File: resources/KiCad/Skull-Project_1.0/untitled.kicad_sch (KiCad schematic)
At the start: 1 part

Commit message: add Microwave Sensor for option two eyes
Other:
- title: Optional 2nd Eye -> Skull-Project 1.0
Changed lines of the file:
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@@
   (paper "A4")
   (title_block
-    (title "Optional 2nd Eye")
+    (title "Skull-Project 1.0")
     (date "2024-09-15")
     (rev "1.0")

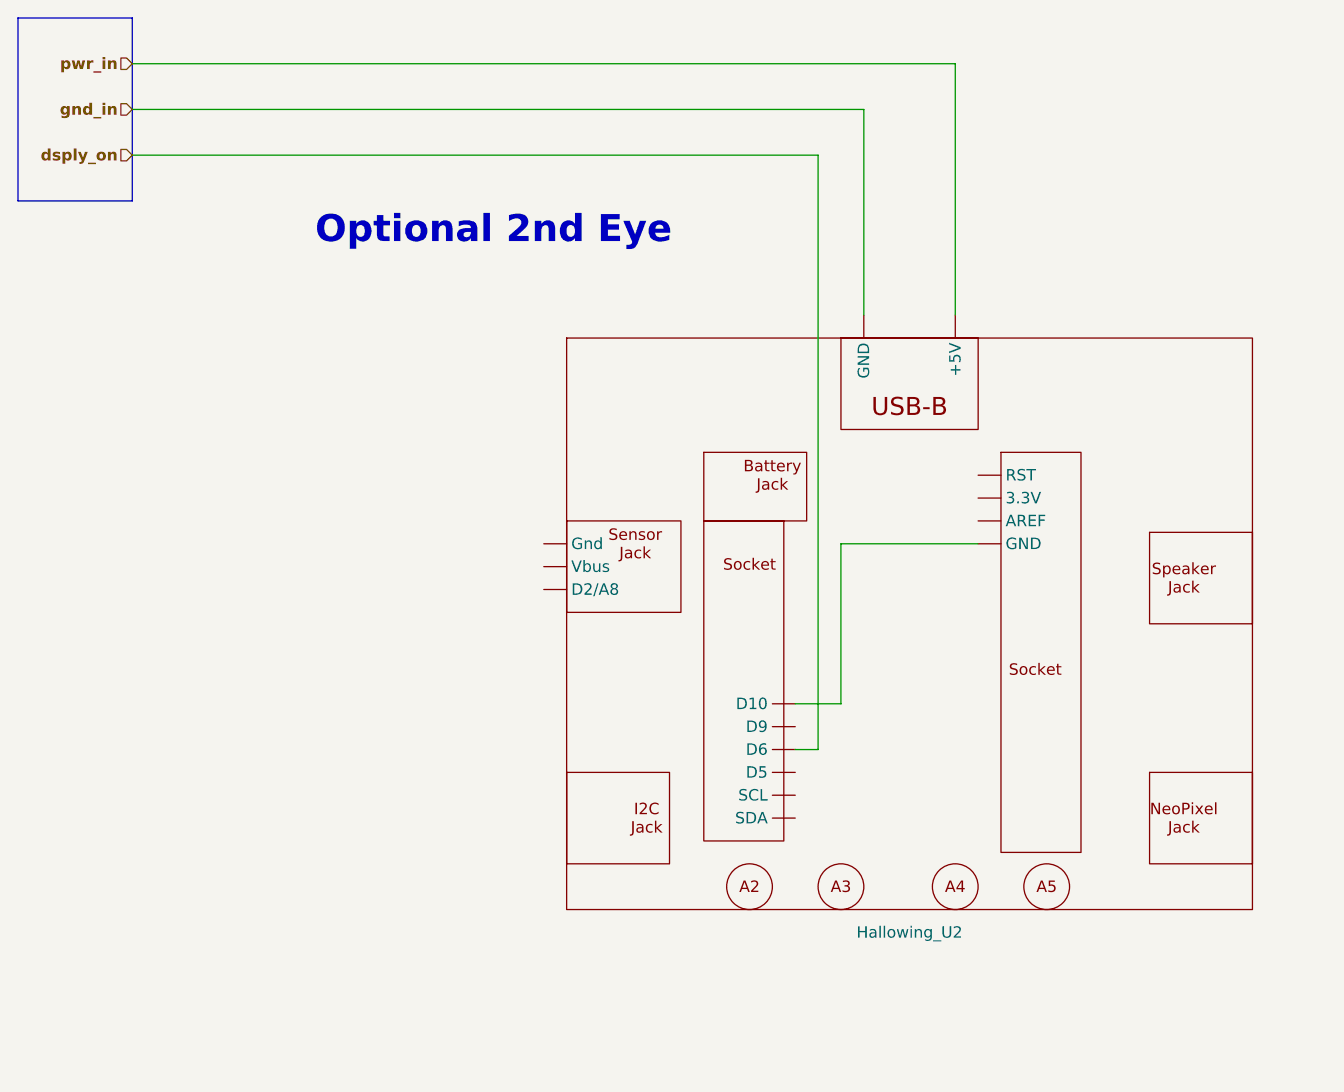
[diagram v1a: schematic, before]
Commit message: clean up schematic
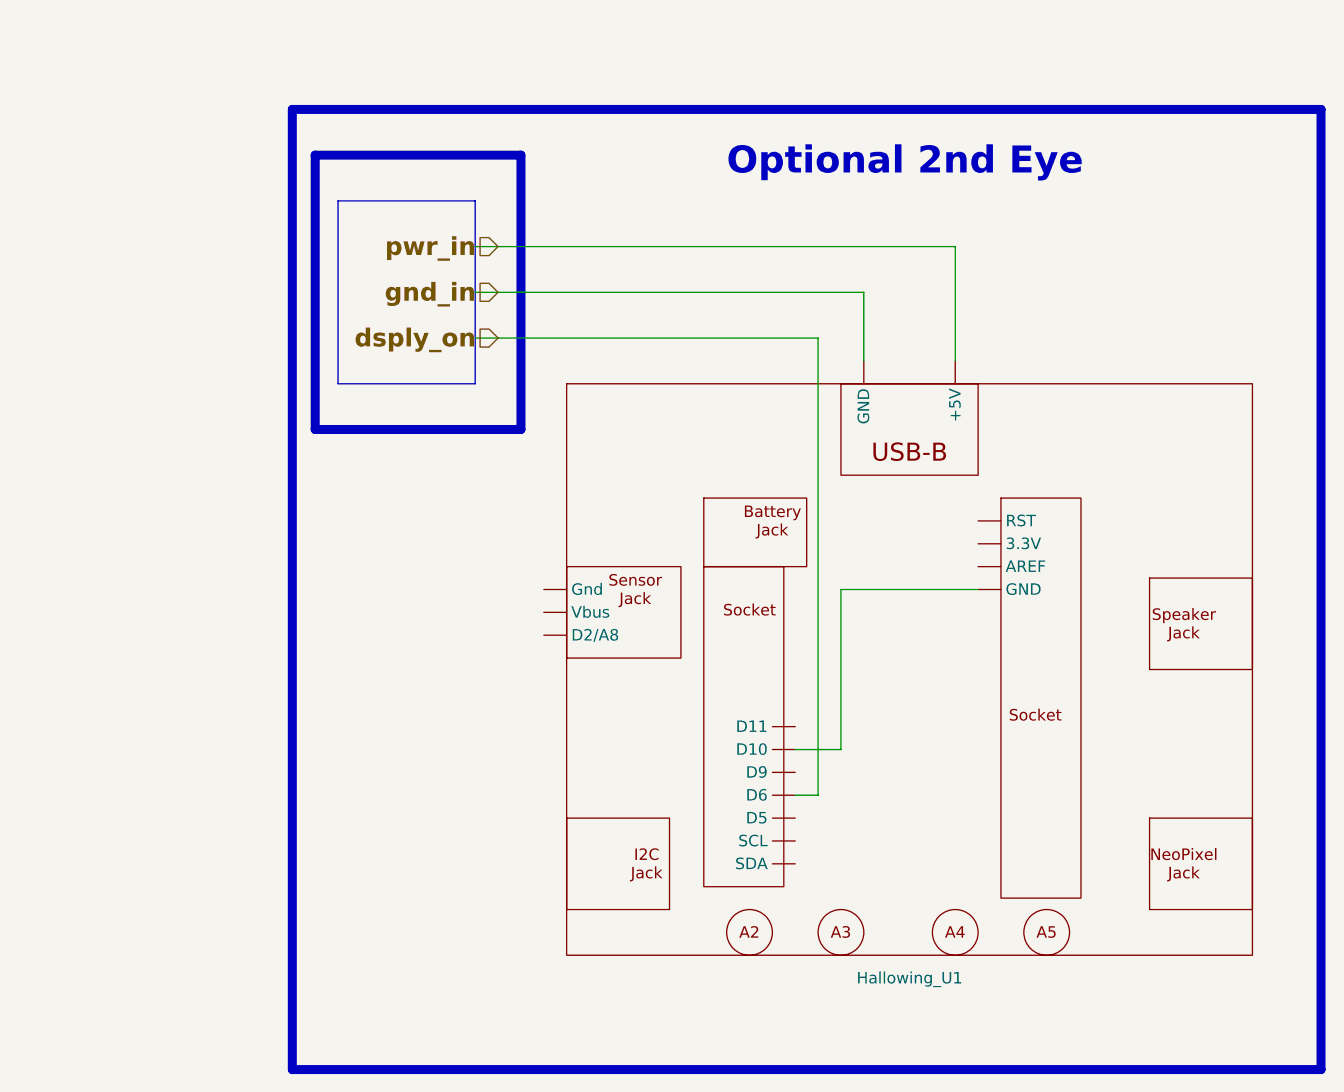
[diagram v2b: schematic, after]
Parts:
- removed Hallowing_U2: ~, symbol mdoLibrary:Hallowing_M4
- added Hallowing_U1: ~, symbol mdoLibrary:Hallowing_M4
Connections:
- net gnd_in: now also Hallowing_U1. (Vbus)
- net pwr_in: now also Hallowing_U1. (Vbus)
- new net dsply_on : Hallowing_U1. (Vbus)
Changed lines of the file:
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@@
     (comment 2 "NOTE: Hallowing as from display side (not connector side)")
   )
-  (wire (pts (xy 152.4 111.76) (xy 147.32 111.76))
+  (wire (pts (xy 152.4 116.84) (xy 147.32 116.84))
     (stroke (width 0) (type default))
   )
-  (wire (pts (xy 167.64 93.98) (xy 152.4 93.98))
+  (wire (pts (xy 165.1 60.96) (xy 165.1 73.66))
     (stroke (width 0) (type default))
   )
-  (wire (pts (xy 73.66 50.8) (xy 149.86 50.8))
+  (wire (pts (xy 167.64 99.06) (xy 152.4 99.06))
     (stroke (width 0) (type default))
   )
-  (wire (pts (xy 73.66 40.64) (xy 165.1 40.64))
+  (wire (pts (xy 149.86 71.12) (xy 149.86 121.92))
     (stroke (width 0) (type default))
   )
-  (wire (pts (xy 73.66 45.72) (xy 154.94 45.72))
+  (wire (pts (xy 111.76 71.12) (xy 149.86 71.12))
     (stroke (width 0) (type default))
   )
-  (wire (pts (xy 152.4 93.98) (xy 152.4 111.76))
+  (wire (pts (xy 152.4 99.06) (xy 152.4 116.84))
     (stroke (width 0) (type default))
   )
-  (wire (pts (xy 165.1 40.64) (xy 165.1 68.58))
+  (wire (pts (xy 111.76 60.96) (xy 165.1 60.96))
     (stroke (width 0) (type default))
   )
-  (wire (pts (xy 154.94 45.72) (xy 154.94 68.58))
+  (wire (pts (xy 154.94 66.04) (xy 154.94 73.66))
     (stroke (width 0) (type default))
   )
-  (wire (pts (xy 149.86 50.8) (xy 149.86 116.84))
+  (wire (pts (xy 111.76 66.04) (xy 154.94 66.04))
     (stroke (width 0) (type default))
   )
-  (wire (pts (xy 147.32 116.84) (xy 149.86 116.84))
+  (wire (pts (xy 147.32 121.92) (xy 149.86 121.92))
     (stroke (width 0) (type default))
   )
-  (rectangle (start 60.96 35.56) (end 73.66 55.88)
+  (rectangle (start 93.98 50.8) (end 116.84 81.28)
+    (stroke (width 1) (type default) (color 255 153 0 1))
+    (fill (type none))
+  )
+  (rectangle (start 96.52 55.88) (end 111.76 76.2)
     (stroke (width 0) (type default))
     (fill (type none))
   )
-  (text "Optional 2nd Eye" (at 93.98 60.96 0)
+  (rectangle (start 91.44 45.72) (end 205.74 152.4)
+    (stroke (width 1) (type default))
+    (fill (type none))
+  )
+  (rectangle (start 101.6 50.8) (end 101.6 50.8)
+    (stroke (width 0) (type default))
+    (fill (type none))
+  )
+  (text "Optional 2nd Eye" (at 139.7 53.34 0)
     (effects (font (size 3 3) (thickness 0.6) bold) (justify left bottom))
   )
-  (hierarchical_label "dsply_on" (shape input) (at 73.66 50.8 180) (fields_autoplaced)
-    (effects (font (size 1.27 1.27) bold) (justify right))
+  (hierarchical_label "dsply_on " (shape input) (at 114.3 71.12 180) (fields_autoplaced)
+    (effects (font (size 2 2) bold) (justify right))
   )
-  (hierarchical_label "gnd_in" (shape input) (at 73.66 45.72 180) (fields_autoplaced)
-    (effects (font (size 1.27 1.27) bold) (justify right))
+  (hierarchical_label "gnd_in" (shape input) (at 114.3 66.04 180) (fields_autoplaced)
+    (effects (font (size 2 2) bold) (justify right))
   )
-  (hierarchical_label "pwr_in" (shape input) (at 73.66 40.64 180) (fields_autoplaced)
-    (effects (font (size 1.27 1.27) bold) (justify right))
+  (hierarchical_label "pwr_in" (shape input) (at 114.3 60.96 180) (fields_autoplaced)
+    (effects (font (size 2 2) bold) (justify right))
   )
-  (symbol (lib_id "mdoLibrary:Hallowing_M4") (at 160.02 71.12 0) (unit 1)
+  (symbol (lib_name "Hallowing_M4_1") (lib_id "mdoLibrary:Hallowing_M4") (at 160.02 76.2 0) (unit 1)
     (in_bom yes) (on_board yes) (dnp no) (fields_autoplaced)
-    (property "Reference" "Hallowing_U2" (at 160.02 137.16 0)
+    (property "Reference" "Hallowing_U1" (at 160.02 142.24 0)
       (effects (font (size 1.27 1.27)))
     )
-    (property "Value" "~" (at 160.02 71.12 0)
+    (property "Value" "~" (at 160.02 76.2 0)
       (effects (font (size 1.27 1.27)))
     )
-    (property "Footprint" "" (at 160.02 71.12 0)
+    (property "Footprint" "" (at 160.02 76.2 0)
       (effects (font (size 1.27 1.27)) hide)
     )
-    (property "Datasheet" "" (at 160.02 71.12 0)
+    (property "Datasheet" "" (at 160.02 76.2 0)
       (effects (font (size 1.27 1.27)) hide)
     )
+    (pin "")
     (pin "")
     (pin "")
@@
       (project "Skull-Project_1.0"
         (path "/13d7b3b4-5d80-4b2f-98bb-c8334b3eaf59/dd2fe223-2832-49f4-937d-cadfea313ce4"
-          (reference "Hallowing_U2") (unit 1)
+          (reference "Hallowing_U1") (unit 1)
         )
       )

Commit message: microwave sensor now uses NANO for edge detect
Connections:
- net gnd_in is gone; now on net pwr_in : Hallowing_U1. (Vbus)
- net pwr_in is gone; now on net pwr_in : Hallowing_U1. (Vbus)
- net pwr_in : now reaches Hallowing_U1. (Vbus)
- new net gnd_in : Hallowing_U1. (Vbus)
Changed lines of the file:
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@@
     (effects (font (size 2 2) bold) (justify right))
   )
-  (hierarchical_label "gnd_in" (shape input) (at 114.3 66.04 180) (fields_autoplaced)
+  (hierarchical_label "gnd_in " (shape input) (at 114.3 66.04 180) (fields_autoplaced)
     (effects (font (size 2 2) bold) (justify right))
   )
-  (hierarchical_label "pwr_in" (shape input) (at 114.3 60.96 180) (fields_autoplaced)
+  (hierarchical_label "pwr_in " (shape input) (at 114.3 60.96 180) (fields_autoplaced)
     (effects (font (size 2 2) bold) (justify right))
   )

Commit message: add wire colors to schematic
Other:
- note added: "Black"
- note added: "Red"
- note added: "White"
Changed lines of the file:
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@@
   (title_block
     (title "Skull-Project 1.0")
-    (date "2024-09-19")
+    (date "2024-09-20")
     (rev "1.0")
     (company "github.com/Mark-MDO47/Skull-Project")
@@
     (fill (type none))
   )
+  (text "Black" (at 160.02 99.06 0)
+    (effects (font (size 1.27 1.27) bold) (justify left bottom))
+  )
+  (text "White" (at 119.38 71.12 0)
+    (effects (font (size 1.27 1.27) bold) (justify left bottom))
+  )
+  (text "Black" (at 119.38 66.04 0)
+    (effects (font (size 1.27 1.27) bold) (justify left bottom))
+  )
+  (text "Red" (at 119.38 60.96 0)
+    (effects (font (size 1.27 1.27) bold) (justify left bottom))
+  )
   (text "Optional 2nd Eye" (at 139.7 53.34 0)
     (effects (font (size 3 3) (thickness 0.6) bold) (justify left bottom))
   )
+  (text "Red" (at 149.86 60.96 0)
+    (effects (font (size 1.27 1.27) bold) (justify left bottom))
+  )
+  (text "White" (at 149.86 93.98 0)
+    (effects (font (size 1.27 1.27) bold) (justify left bottom))
+  )
+  (text "Black" (at 149.86 66.04 0)
+    (effects (font (size 1.27 1.27) bold) (justify left bottom))
+  )
   (hierarchical_label "dsply_on " (shape input) (at 114.3 71.12 180) (fields_autoplaced)

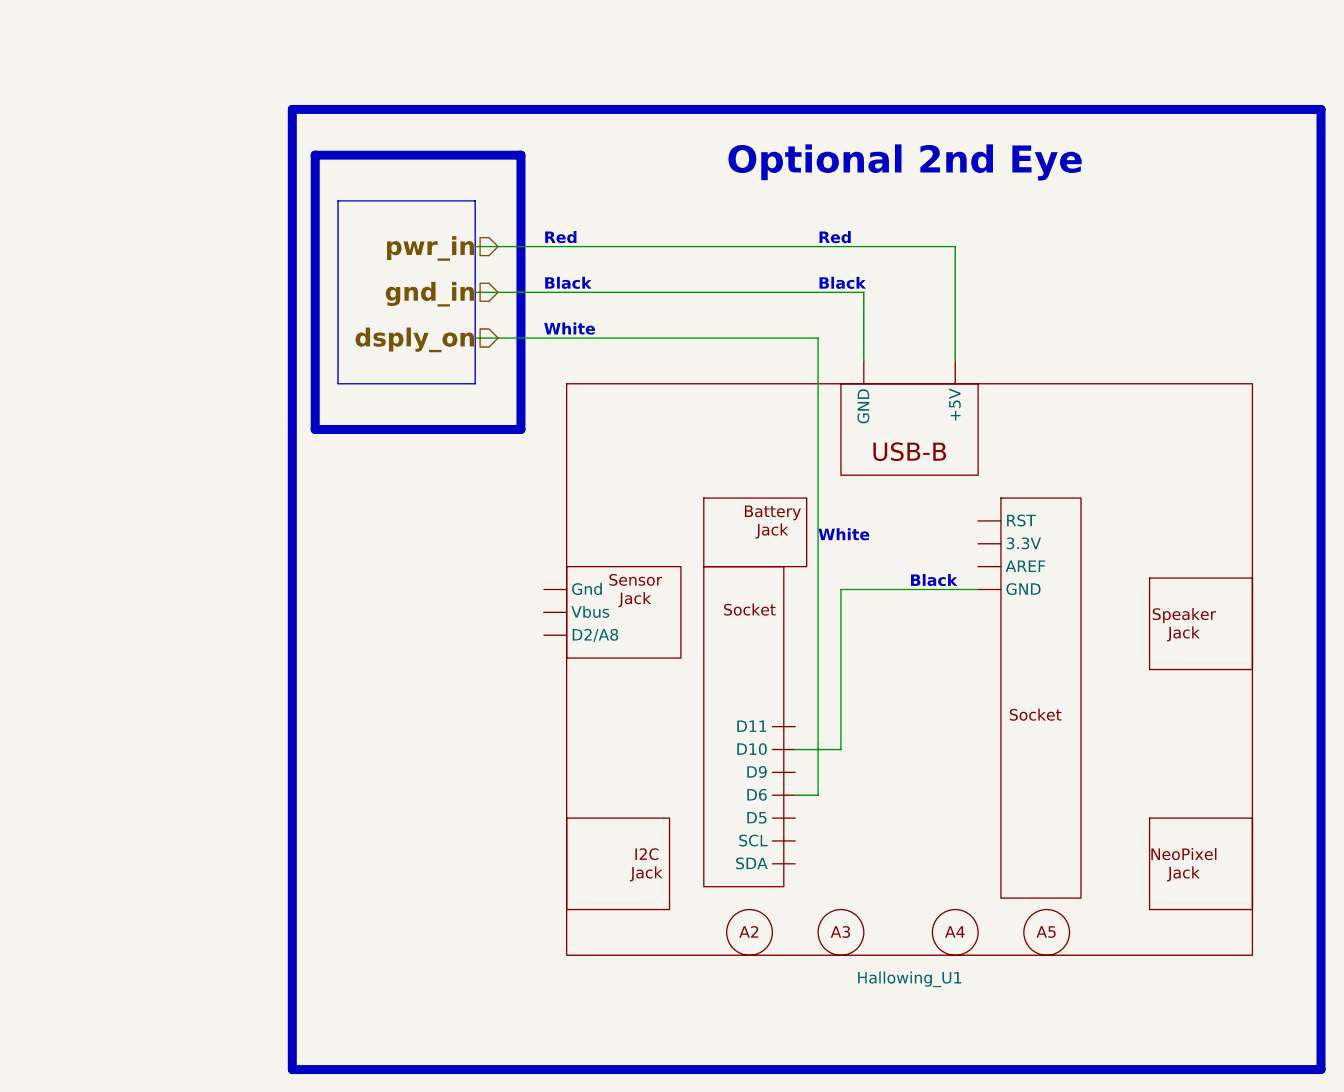
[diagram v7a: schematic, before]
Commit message: schematic uses 4pin cable for power, details on internal skull cabling
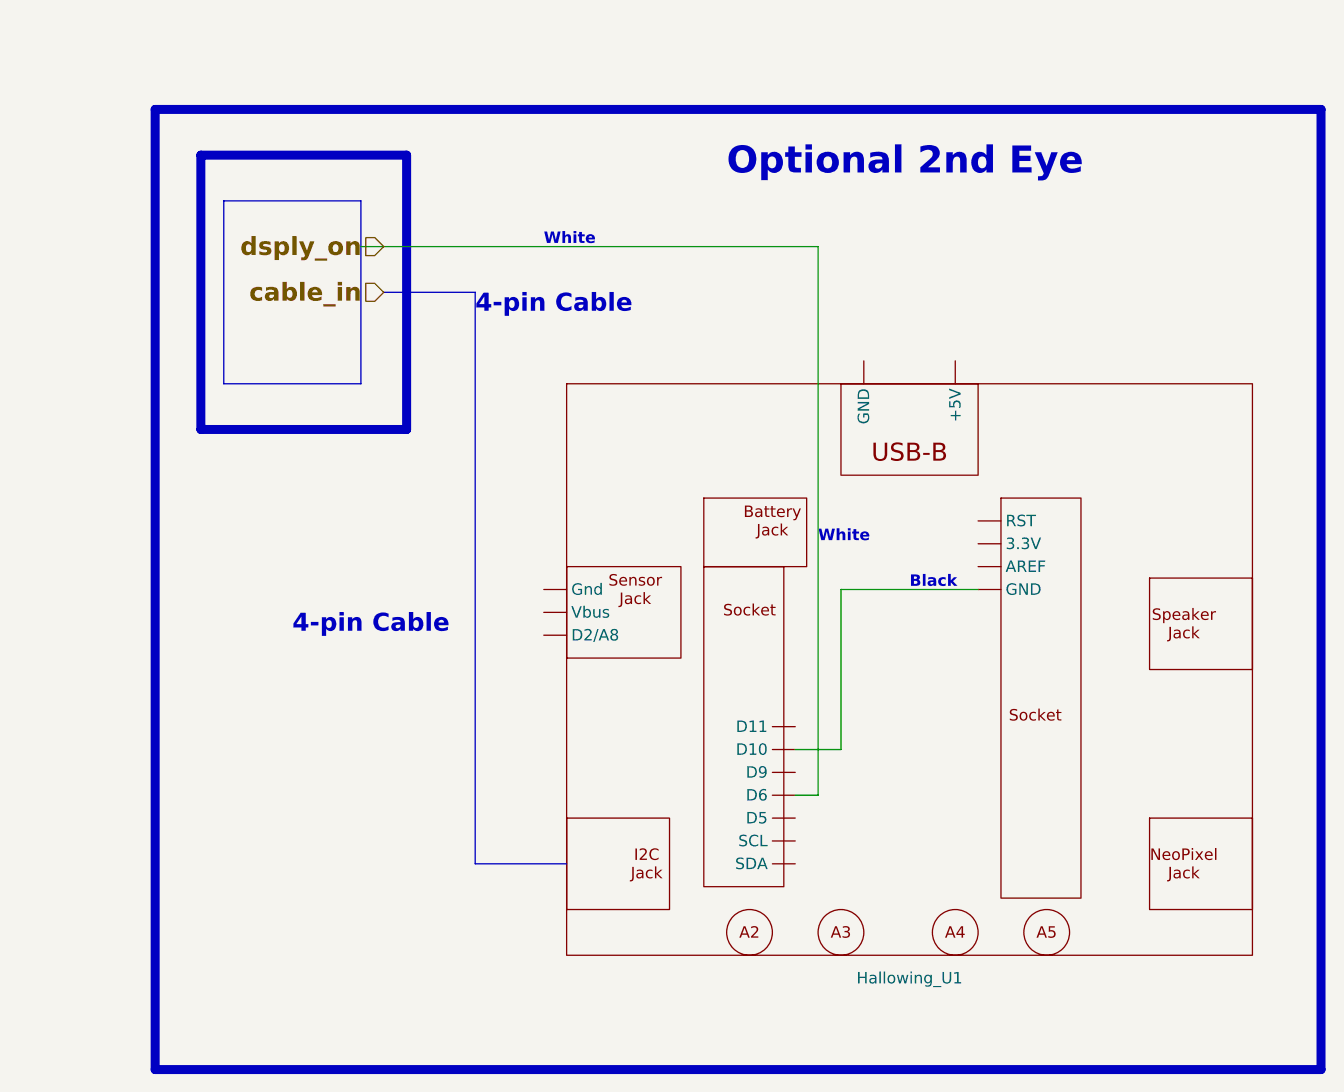
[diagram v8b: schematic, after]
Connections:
- net gnd_in  is gone; now on net dsply_on : Hallowing_U1. (Vbus)
- net pwr_in  is gone; now on net dsply_on : Hallowing_U1. (Vbus)
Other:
- note added: "4-pin Cable"
- note removed: "Red"
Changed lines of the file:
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@@
   (title_block
     (title "Skull-Project 1.0")
-    (date "2024-09-20")
+    (date "2024-09-25")
     (rev "1.0")
     (company "github.com/Mark-MDO47/Skull-Project")
@@
     (stroke (width 0) (type default))
   )
-  (wire (pts (xy 165.1 60.96) (xy 165.1 73.66))
+  (bus (pts (xy 111.76 66.04) (xy 111.76 129.54))
     (stroke (width 0) (type default))
   )
@@
     (stroke (width 0) (type default))
   )
-  (wire (pts (xy 149.86 71.12) (xy 149.86 121.92))
+  (wire (pts (xy 149.86 60.96) (xy 149.86 121.92))
     (stroke (width 0) (type default))
   )
-  (wire (pts (xy 111.76 71.12) (xy 149.86 71.12))
+  (bus (pts (xy 101.6 66.04) (xy 111.76 66.04))
+    (stroke (width 0) (type default))
+  )
+  (bus (pts (xy 111.76 129.54) (xy 121.92 129.54))
+    (stroke (width 0) (type default))
+  )
+  (wire (pts (xy 99.06 60.96) (xy 149.86 60.96))
     (stroke (width 0) (type default))
   )
@@
     (stroke (width 0) (type default))
   )
-  (wire (pts (xy 111.76 60.96) (xy 165.1 60.96))
-    (stroke (width 0) (type default))
-  )
-  (wire (pts (xy 154.94 66.04) (xy 154.94 73.66))
-    (stroke (width 0) (type default))
-  )
-  (wire (pts (xy 111.76 66.04) (xy 154.94 66.04))
-    (stroke (width 0) (type default))
-  )
   (wire (pts (xy 147.32 121.92) (xy 149.86 121.92))
     (stroke (width 0) (type default))
   )
-  (rectangle (start 93.98 50.8) (end 116.84 81.28)
+  (rectangle (start 81.28 50.8) (end 104.14 81.28)
     (stroke (width 1) (type default) (color 255 153 0 1))
     (fill (type none))
   )
-  (rectangle (start 96.52 55.88) (end 111.76 76.2)
+  (rectangle (start 83.82 55.88) (end 99.06 76.2)
     (stroke (width 0) (type default))
     (fill (type none))
   )
-  (rectangle (start 91.44 45.72) (end 205.74 152.4)
+  (rectangle (start 76.2 45.72) (end 205.74 152.4)
     (stroke (width 1) (type default))
     (fill (type none))
   )
-  (rectangle (start 101.6 50.8) (end 101.6 50.8)
+  (rectangle (start 88.9 50.8) (end 88.9 50.8)
     (stroke (width 0) (type default))
     (fill (type none))
@@
     (effects (font (size 1.27 1.27) bold) (justify left bottom))
   )
-  (text "White" (at 119.38 71.12 0)
+  (text "White" (at 119.38 60.96 0)
     (effects (font (size 1.27 1.27) bold) (justify left bottom))
   )
-  (text "Black" (at 119.38 66.04 0)
-    (effects (font (size 1.27 1.27) bold) (justify left bottom))
+  (text "4-pin Cable" (at 111.76 68.58 0)
+    (effects (font (size 2 2) bold) (justify left bottom))
   )
-  (text "Red" (at 119.38 60.96 0)
-    (effects (font (size 1.27 1.27) bold) (justify left bottom))
+  (text "4-pin Cable" (at 91.44 104.14 0)
+    (effects (font (size 2 2) bold) (justify left bottom))
   )
   (text "Optional 2nd Eye" (at 139.7 53.34 0)
     (effects (font (size 3 3) (thickness 0.6) bold) (justify left bottom))
   )
-  (text "Red" (at 149.86 60.96 0)
-    (effects (font (size 1.27 1.27) bold) (justify left bottom))
-  )
   (text "White" (at 149.86 93.98 0)
     (effects (font (size 1.27 1.27) bold) (justify left bottom))
   )
-  (text "Black" (at 149.86 66.04 0)
-    (effects (font (size 1.27 1.27) bold) (justify left bottom))
-  )
-  (hierarchical_label "dsply_on " (shape input) (at 114.3 71.12 180) (fields_autoplaced)
+  (hierarchical_label "dsply_on " (shape input) (at 101.6 60.96 180) (fields_autoplaced)
     (effects (font (size 2 2) bold) (justify right))
   )
-  (hierarchical_label "gnd_in " (shape input) (at 114.3 66.04 180) (fields_autoplaced)
+  (hierarchical_label "cable_in " (shape input) (at 101.6 66.04 180) (fields_autoplaced)
     (effects (font (size 2 2) bold) (justify right))
   )
-  (hierarchical_label "pwr_in " (shape input) (at 114.3 60.96 180) (fields_autoplaced)
-    (effects (font (size 2 2) bold) (justify right))
-  )
